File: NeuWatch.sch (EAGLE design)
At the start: 65 parts, among them IC1 SAMD21G18A-AUT, IC3 TPS2115, IC4 SIP32401A, IC5 MC74VHC1G14DFT, T1 846, T2 2N7002_ALT, Y1 32,768Khz

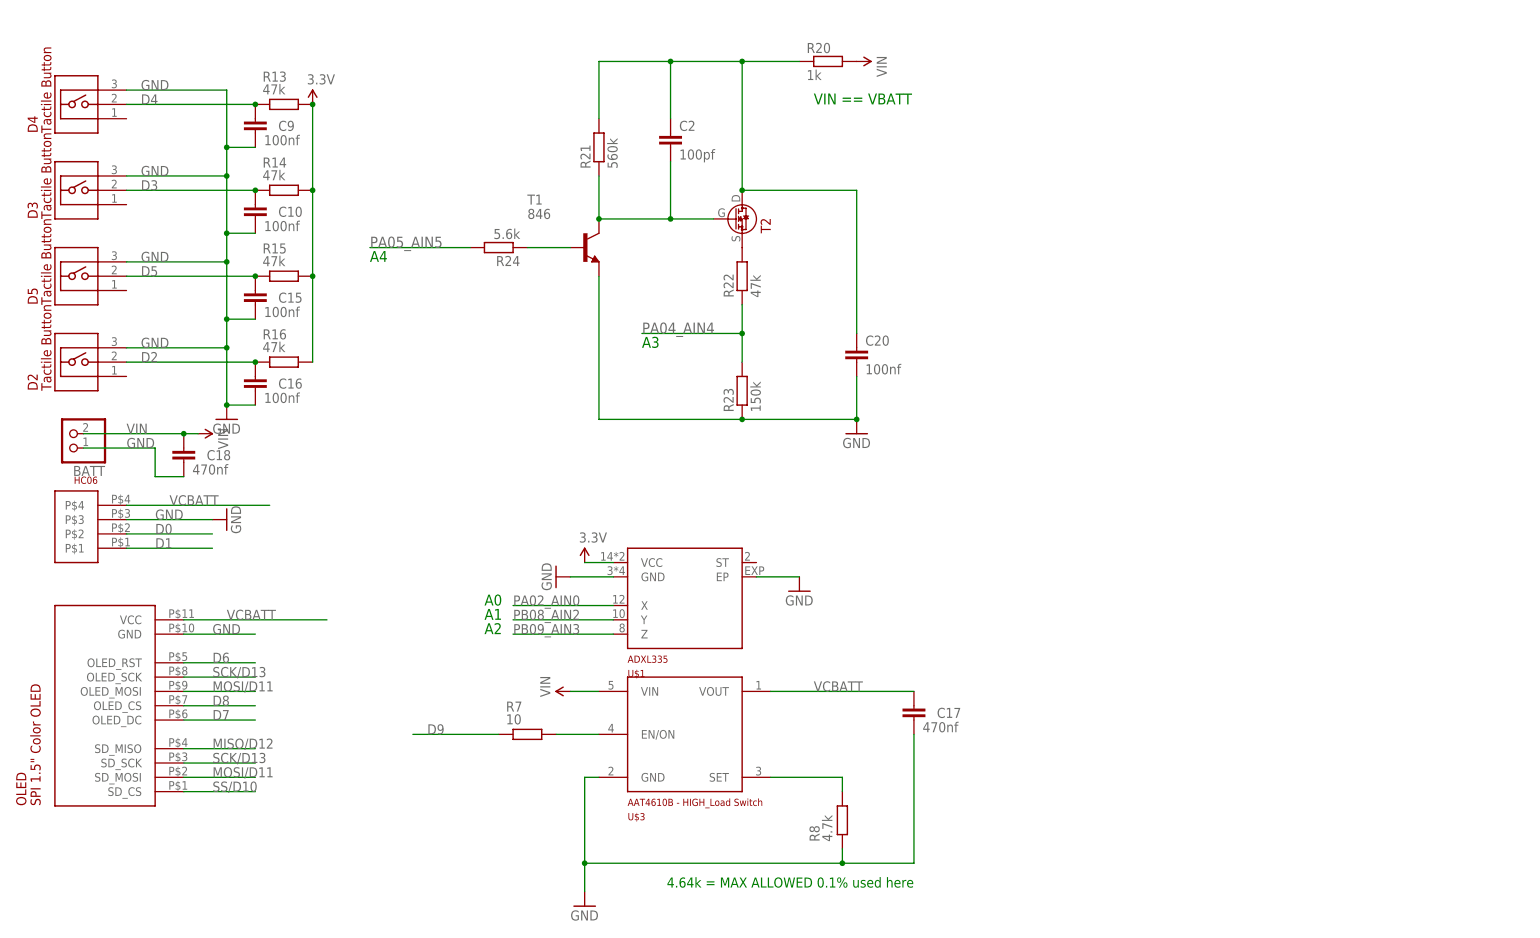
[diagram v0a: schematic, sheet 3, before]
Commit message: vin control
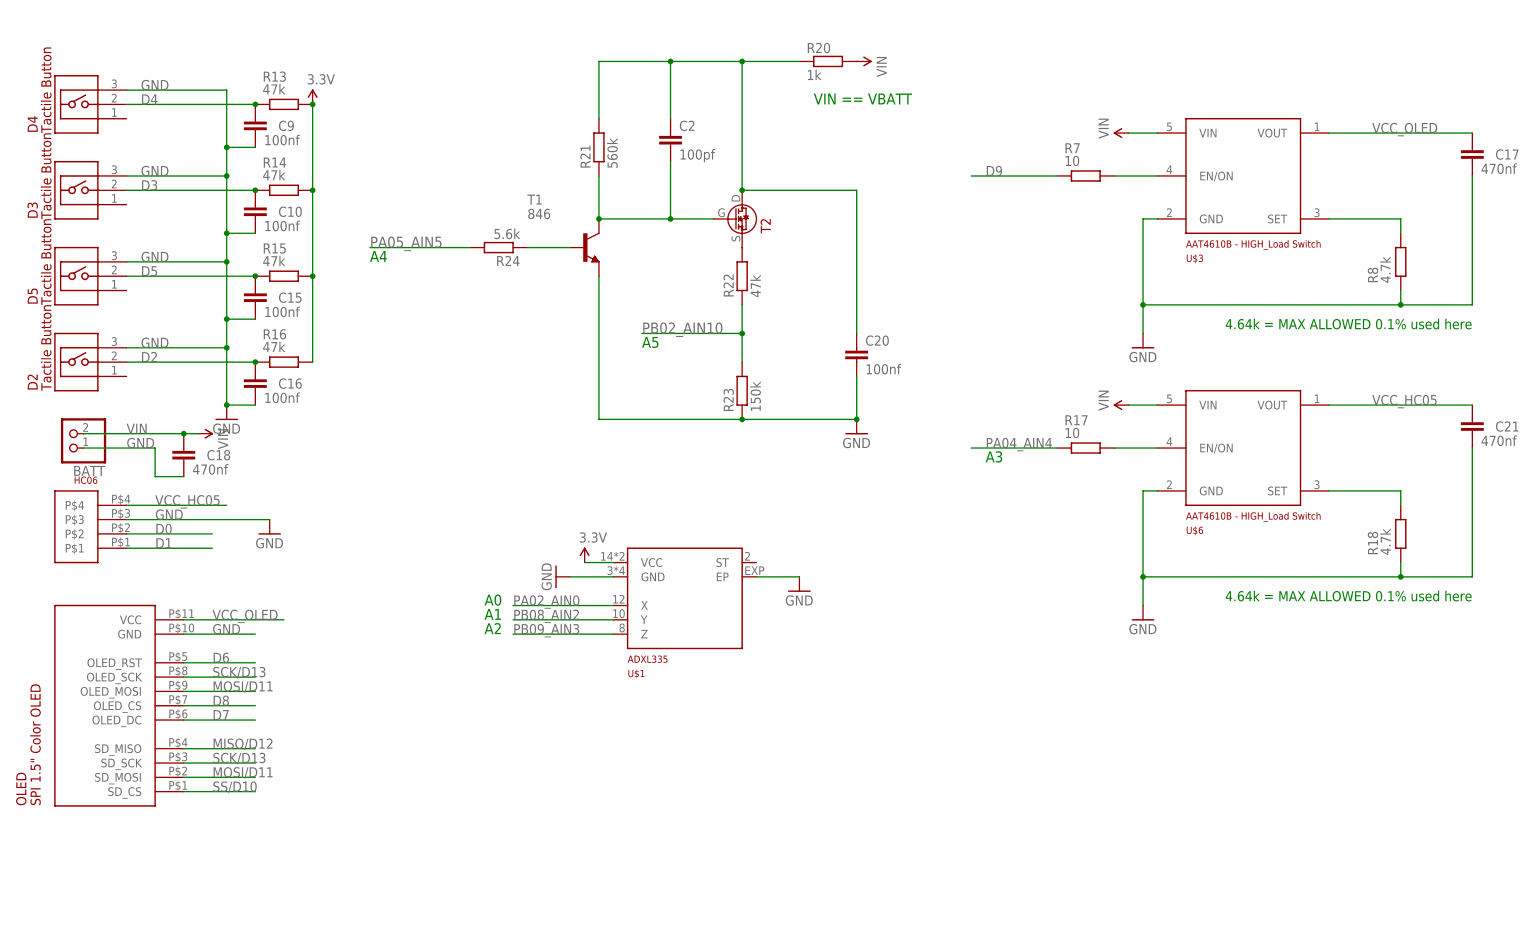
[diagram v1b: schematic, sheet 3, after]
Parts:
- added C21: 470nf, AtomTech:CAPACITORC0402
- added R17: 10, rcl:R-EU_R0402
- added R18: 4.7k, rcl:R-EU_R0402
- added U$6: AAT4610B, AtomTech:AAT4610B
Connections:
- removed net VCBATT: C17.1, HC06.P$4, OLED.VCC, U$3.VOUT
- new net N$12: R17.2, U$6.EN/ON
- new net N$13: R18.2, U$6.SET
- new net VCC_HC05: C21.1, HC06.P$4, U$6.VOUT
- new net VCC_OLED: C17.1, OLED.VCC, U$3.VOUT
- net GND: now also C21.2, R18.1, U$6.GND
- net PA04_AIN4: now also R17.1; no longer R22.1, R23.2
- net PB02_AIN10: now also R22.1, R23.2
- net VIN: now also U$6.VIN
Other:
- note added: "A5"
- moved on the sheet: C17, R7, R8, U$3

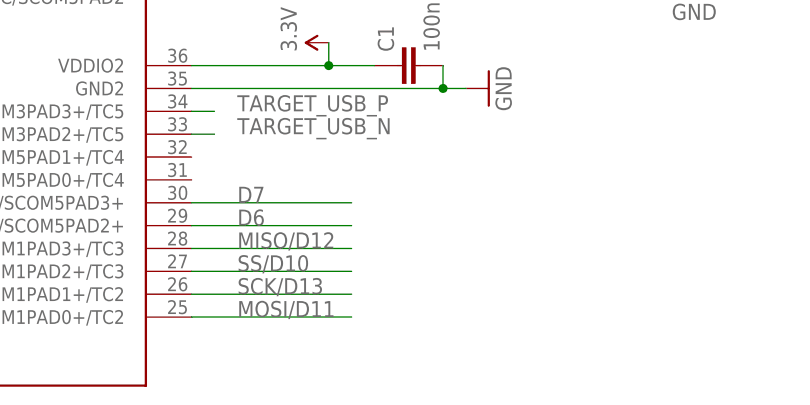
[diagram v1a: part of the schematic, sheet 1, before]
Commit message: CLR SPI
Current Limiting Resistors added to SPI
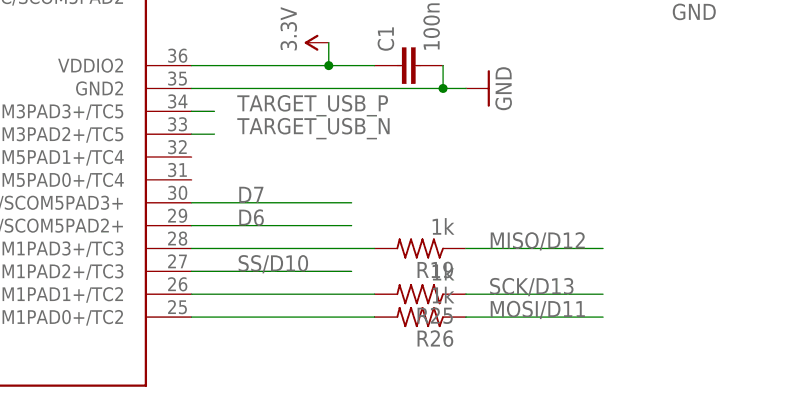
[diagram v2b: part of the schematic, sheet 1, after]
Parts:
- added R19, R25, R26: 1k, adafruit:R-US_R0402
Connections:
- new net N$15: IC1.PA19/EIC/SCOM1PAD3+/TC3, R19.2
- new net N$16: IC1.PA17/I2C/EIC/SCOM1PAD1+/TC2, R25.2
- new net N$17: IC1.PA16/I2C/EIC/SCOM1PAD0+/TC2, R26.2
- net MISO/D12: now also R19.1; no longer IC1.PA19/EIC/SCOM1PAD3+/TC3
- net MOSI/D11: now also R26.1; no longer IC1.PA16/I2C/EIC/SCOM1PAD0+/TC2
- net SCK/D13: now also R25.1; no longer IC1.PA17/I2C/EIC/SCOM1PAD1+/TC2
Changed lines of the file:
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@@
 <part name="R18" library="rcl" deviceset="R-EU_" device="R0402" value="4.7k"/>
 <part name="C21" library="AtomTech" deviceset="CAPACITOR" device="C0402" value="470nf"/>
+<part name="R19" library="adafruit" deviceset="R-US_" device="R0402" value="1k"/>
+<part name="R25" library="adafruit" deviceset="R-US_" device="R0402" value="1k"/>
+<part name="R26" library="adafruit" deviceset="R-US_" device="R0402" value="1k"/>
 </parts>
 <sheets>
@@
 <instance part="RESET" gate="G$1" x="157.48" y="203.2" rot="R90"/>
 <instance part="C19" gate="G$1" x="269.24" y="124.46"/>
+<instance part="R19" gate="G$1" x="238.76" y="88.9" rot="R180"/>
+<instance part="R25" gate="G$1" x="238.76" y="83.82" rot="R180"/>
+<instance part="R26" gate="G$1" x="238.76" y="81.28" rot="R180"/>
 </instances>
 <busses>
@@
 <net name="MOSI/D11" class="0">
 <segment>
-<pinref part="IC1" gate="G$1" pin="PA16/I2C/EIC/SCOM1PAD0+/TC2"/>
-<wire x1="213.36" y1="81.28" x2="231.14" y2="81.28" width="0.1524" layer="91"/>
-<label x="218.44" y="81.28" size="1.778" layer="95"/>
+<wire x1="243.84" y1="81.28" x2="259.08" y2="81.28" width="0.1524" layer="91"/>
+<label x="246.38" y="81.28" size="1.778" layer="95"/>
+<pinref part="R26" gate="G$1" pin="1"/>
 </segment>
 </net>
 <net name="MISO/D12" class="0">
 <segment>
-<pinref part="IC1" gate="G$1" pin="PA19/EIC/SCOM1PAD3+/TC3"/>
-<wire x1="213.36" y1="88.9" x2="231.14" y2="88.9" width="0.1524" layer="91"/>
-<label x="218.44" y="88.9" size="1.778" layer="95"/>
+<wire x1="243.84" y1="88.9" x2="259.08" y2="88.9" width="0.1524" layer="91"/>
+<label x="246.38" y="88.9" size="1.778" layer="95"/>
+<pinref part="R19" gate="G$1" pin="1"/>
 </segment>
 </net>
@@
 <net name="SCK/D13" class="0">
 <segment>
+<wire x1="243.84" y1="83.82" x2="259.08" y2="83.82" width="0.1524" layer="91"/>
+<label x="246.38" y="83.82" size="1.778" layer="95"/>
+<pinref part="R25" gate="G$1" pin="1"/>
+</segment>
+</net>
+<net name="N$15" class="0">
+<segment>
+<pinref part="IC1" gate="G$1" pin="PA19/EIC/SCOM1PAD3+/TC3"/>
+<pinref part="R19" gate="G$1" pin="2"/>
+<wire x1="233.68" y1="88.9" x2="213.36" y2="88.9" width="0.1524" layer="91"/>
+</segment>
+</net>
+<net name="N$16" class="0">
+<segment>
 <pinref part="IC1" gate="G$1" pin="PA17/I2C/EIC/SCOM1PAD1+/TC2"/>
-<wire x1="213.36" y1="83.82" x2="231.14" y2="83.82" width="0.1524" layer="91"/>
-<label x="218.44" y="83.82" size="1.778" layer="95"/>
-</segment>
-</net>
+<pinref part="R25" gate="G$1" pin="2"/>
+<wire x1="233.68" y1="83.82" x2="213.36" y2="83.82" width="0.1524" layer="91"/>
+</segment>
+</net>
+<net name="N$17" class="0">
+<segment>
+<pinref part="IC1" gate="G$1" pin="PA16/I2C/EIC/SCOM1PAD0+/TC2"/>
+<pinref part="R26" gate="G$1" pin="2"/>
+<wire x1="233.68" y1="81.28" x2="213.36" y2="81.28" width="0.1524" layer="91"/>
+</segment>
+</net>

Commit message: added CLR again
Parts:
- added R27, R28, R29: 1k, adafruit:R-US_R0402
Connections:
- new net N$18: IC1.PA20/EIC/SCOM5PAD2+, R28.2
- new net N$19: IC1.PA21/EIC/SCOM5PAD3+, R27.2
- new net N$20: IC1.PA6/EIC/AIN6/SCOM0PAD2/TC1, R29.1
- net D6: now also R28.1; no longer IC1.PA20/EIC/SCOM5PAD2+
- net D7: now also R27.1; no longer IC1.PA21/EIC/SCOM5PAD3+
- net D8: now also R29.2; no longer IC1.PA6/EIC/AIN6/SCOM0PAD2/TC1
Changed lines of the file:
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@@
 <part name="R25" library="adafruit" deviceset="R-US_" device="R0402" value="1k"/>
 <part name="R26" library="adafruit" deviceset="R-US_" device="R0402" value="1k"/>
+<part name="R27" library="adafruit" deviceset="R-US_" device="R0402" value="1k"/>
+<part name="R28" library="adafruit" deviceset="R-US_" device="R0402" value="1k"/>
+<part name="R29" library="adafruit" deviceset="R-US_" device="R0402" value="1k"/>
 </parts>
 <sheets>
@@
 <instance part="R25" gate="G$1" x="238.76" y="83.82" rot="R180"/>
 <instance part="R26" gate="G$1" x="238.76" y="81.28" rot="R180"/>
+<instance part="R27" gate="G$1" x="238.76" y="93.98" rot="R180"/>
+<instance part="R28" gate="G$1" x="238.76" y="91.44" rot="R180"/>
+<instance part="R29" gate="G$1" x="119.38" y="119.38" rot="R180"/>
 </instances>
 <busses>
@@
 <net name="D6" class="0">
 <segment>
-<pinref part="IC1" gate="G$1" pin="PA20/EIC/SCOM5PAD2+"/>
-<wire x1="213.36" y1="91.44" x2="231.14" y2="91.44" width="0.1524" layer="91"/>
-<label x="218.44" y="91.44" size="1.778" layer="95"/>
+<wire x1="243.84" y1="91.44" x2="261.62" y2="91.44" width="0.1524" layer="91"/>
+<label x="248.92" y="91.44" size="1.778" layer="95"/>
+<pinref part="R28" gate="G$1" pin="1"/>
 </segment>
 </net>
@@
 <net name="D7" class="0">
 <segment>
-<pinref part="IC1" gate="G$1" pin="PA21/EIC/SCOM5PAD3+"/>
-<wire x1="213.36" y1="93.98" x2="231.14" y2="93.98" width="0.1524" layer="91"/>
-<label x="218.44" y="93.98" size="1.778" layer="95"/>
+<wire x1="243.84" y1="93.98" x2="261.62" y2="93.98" width="0.1524" layer="91"/>
+<label x="248.92" y="93.98" size="1.778" layer="95"/>
+<pinref part="R27" gate="G$1" pin="1"/>
 </segment>
 </net>
@@
 <net name="D8" class="0">
 <segment>
-<pinref part="IC1" gate="G$1" pin="PA6/EIC/AIN6/SCOM0PAD2/TC1"/>
-<wire x1="124.46" y1="119.38" x2="106.68" y2="119.38" width="0.1524" layer="91"/>
+<wire x1="114.3" y1="119.38" x2="106.68" y2="119.38" width="0.1524" layer="91"/>
 <label x="106.68" y="119.38" size="1.778" layer="95"/>
+<pinref part="R29" gate="G$1" pin="2"/>
 </segment>
 </net>
@@
 <pinref part="R19" gate="G$1" pin="2"/>
 <wire x1="233.68" y1="88.9" x2="213.36" y2="88.9" width="0.1524" layer="91"/>
+<label x="220.98" y="88.9" size="1.778" layer="95"/>
 </segment>
 </net>
@@
 <pinref part="R25" gate="G$1" pin="2"/>
 <wire x1="233.68" y1="83.82" x2="213.36" y2="83.82" width="0.1524" layer="91"/>
+<label x="220.98" y="83.82" size="1.778" layer="95"/>
 </segment>
 </net>
@@
 <pinref part="R26" gate="G$1" pin="2"/>
 <wire x1="233.68" y1="81.28" x2="213.36" y2="81.28" width="0.1524" layer="91"/>
-</segment>
-</net>
+<label x="220.98" y="81.28" size="1.778" layer="95"/>
+</segment>
+</net>
+<net name="N$18" class="0">
+<segment>
+<pinref part="IC1" gate="G$1" pin="PA20/EIC/SCOM5PAD2+"/>
+<pinref part="R28" gate="G$1" pin="2"/>
+<wire x1="213.36" y1="91.44" x2="233.68" y2="91.44" width="0.1524" layer="91"/>
+<label x="220.98" y="91.44" size="1.778" layer="95"/>
+</segment>
+</net>
+<net name="N$19" class="0">
+<segment>
+<pinref part="R27" gate="G$1" pin="2"/>
+<pinref part="IC1" gate="G$1" pin="PA21/EIC/SCOM5PAD3+"/>
+<wire x1="233.68" y1="93.98" x2="213.36" y2="93.98" width="0.1524" layer="91"/>
+<label x="220.98" y="93.98" size="1.778" layer="95"/>
+</segment>
+</net>
+<net name="N$20" class="0">
+<segment>
+<pinref part="IC1" gate="G$1" pin="PA6/EIC/AIN6/SCOM0PAD2/TC1"/>
+<pinref part="R29" gate="G$1" pin="1"/>
+</segment>
+</net>

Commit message: info
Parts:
- T2: value 2N7002_ALT -> 2N7002
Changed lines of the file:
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@@
 <part name="T1" library="transistor" deviceset="*-NPN-" device="SOT23-BEC" technology="BC846BLT1" value="846"/>
 <part name="R24" library="rcl" deviceset="R-EU_" device="R0402" value="5.6k "/>
-<part name="T2" library="AtomTech" deviceset="2N7002_ALT" device=""/>
+<part name="T2" library="AtomTech" deviceset="2N7002_ALT" device="" value="2N7002"/>
 <part name="SUPPLY3" library="SparkFun-Aesthetics" deviceset="VIN" device=""/>
 <part name="GND1" library="supply1" deviceset="GND" device=""/>

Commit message: updates
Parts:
- L1: value 120 nH -> 1.5 uH
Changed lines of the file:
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@@
 <part name="GND22" library="supply1" deviceset="GND" device=""/>
 <part name="GND23" library="supply1" deviceset="GND" device=""/>
-<part name="L1" library="Bourns_By_element14_Batch_1" deviceset="PM0603-R12J-RC" device="" value="120 nH"/>
+<part name="L1" library="Bourns_By_element14_Batch_1" deviceset="PM0603-R12J-RC" device="" value="1.5 uH"/>
 <part name="C14" library="AtomTech" deviceset="CAPACITOR" device="C0402" value="10 uF"/>
 <part name="GND24" library="supply1" deviceset="GND" device=""/>

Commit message: R6 fix
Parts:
- R6: value 330 -> 30
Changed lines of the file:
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@@
 <part name="GND46" library="supply1" deviceset="GND" device=""/>
 <part name="GND25" library="supply1" deviceset="GND" device=""/>
-<part name="R6" library="adafruit" deviceset="R-US_" device="R0402" value="330"/>
+<part name="R6" library="adafruit" deviceset="R-US_" device="R0402" value="30"/>
 <part name="C1" library="AtomTech" deviceset="CAPACITOR" device="C0402" value="100nF"/>
 <part name="R1" library="adafruit" deviceset="R-US_" device="R0402" value="100K"/>
